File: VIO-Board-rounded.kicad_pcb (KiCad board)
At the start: 4 copper layers, 39.6 x 39.6 mm, 20 parts, among them J1 Conn_01x02_Female, J2 USB_B_Micro, J3 Conn_01x09_Male, J4 Conn_01x09_Male, J5 Conn_01x09_Male, J6 Conn_01x09_Female, J7 Conn_01x09_Female, J8 Conn_01x09_Female, U1 CP2102N-Axx-xQFN28

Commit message: ...
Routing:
- net /SYNC: track 52.6 -> 62.0 mm
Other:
- board text removed: "3v3"
- board text removed: "5v"
- board text removed: "GND"
- board text removed: "OPTO_GND"
- board text removed: "OPTO_IN"
- board text removed: "OPTO_OUT"
- board text removed: "RESTORE"
- board text removed: "RX1"
- board text removed: "RX2"
- board text removed: "SYNC"
- board text removed: "SYNC_IN"
- board text removed: "SYNC_OUT"
- board text removed: "TX"
- board text removed: "TX1"
- board text removed: "TX2"
- board text removed: "VS"

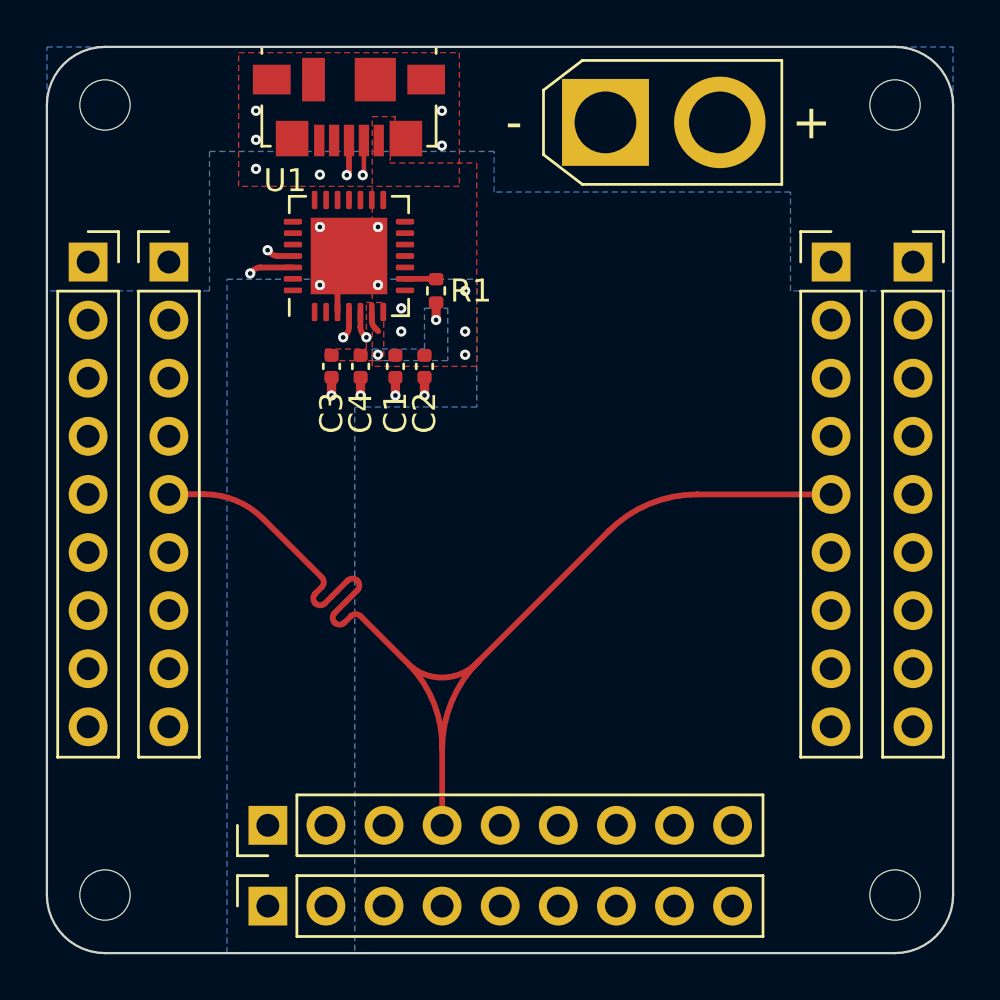
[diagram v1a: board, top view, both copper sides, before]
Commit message: new package, ESD protection, fixes
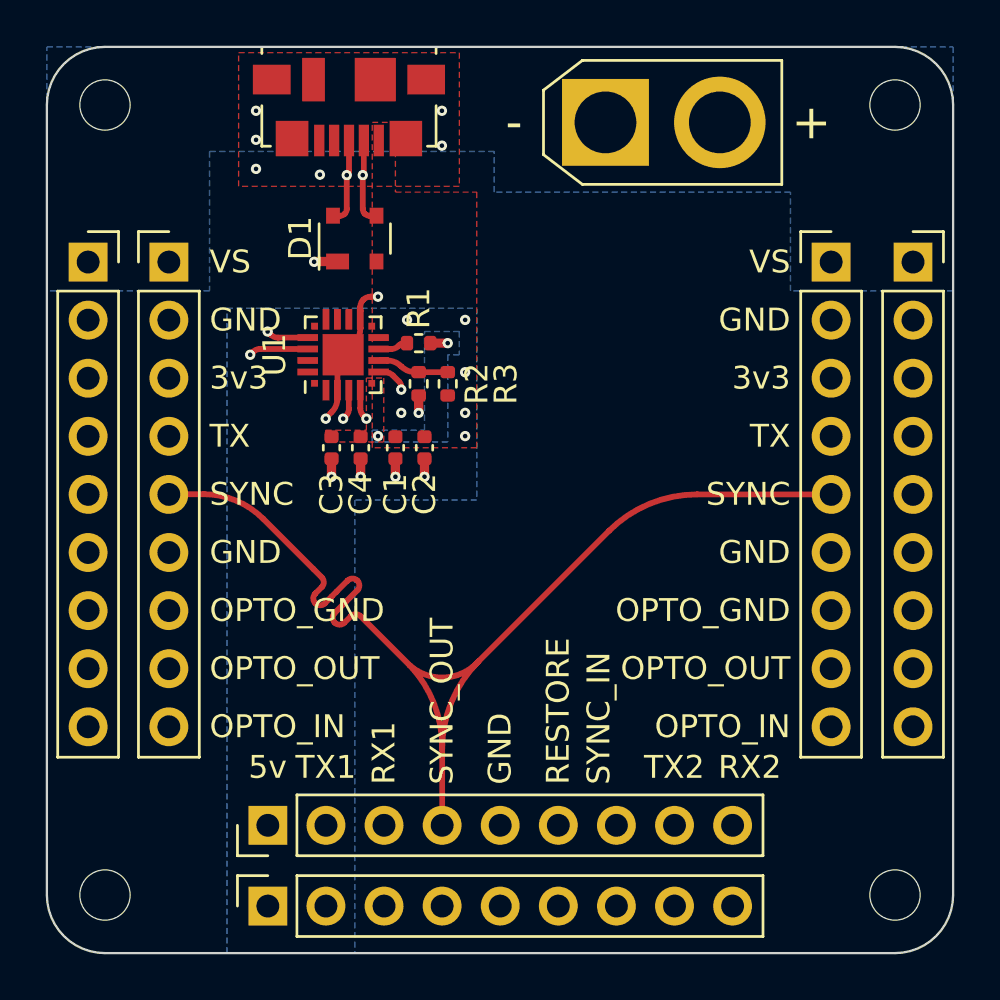
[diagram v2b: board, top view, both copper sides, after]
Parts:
- added D1: SP0503BAHT, Package_TO_SOT_SMD:SOT-143, F.Cu at (70.1, 59.2)
- added R2: 22k1, Resistor_SMD:R_0402_1005Metric, F.Cu at (74.2, 65.5)
- added R3: 47k5, Resistor_SMD:R_0402_1005Metric, F.Cu at (72.9, 65.5)
- U1: value CP2102N-Axx-xQFN28 -> CP2102N-Axx-xQFN20; footprint Package_DFN_QFN:QFN-28-1EP_5x5mm_P0.5mm_EP3.35x3.35mm -> Package_DFN_QFN:SiliconLabs_QFN-20-1EP_3x3mm_P0.5mm_EP1.8x1.8mm
- moved U1 4.33 mm to (69.6, 64.3)
- moved C1 3.56 mm to (71.9, 68.3)
- moved C2 3.56 mm to (73.2, 68.3)
- moved C3 3.56 mm to (69.1, 68.3)
- moved C4 3.56 mm to (70.4, 68.3)
- moved R1 2.41 mm to (72.9, 63.8), turned to 180 degrees
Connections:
- U1 pad 12: unconnected-(U1-Pad12) -> GNDREF
- U1 pad 17: unconnected-(U1-Pad17) -> /RX2
- U1 pad 18: unconnected-(U1-Pad18) -> /TX2
- U1 pad 21: unconnected-(U1-Pad21) -> GNDREF
- U1 pad 8: VBUS -> Net-(R2-Pad2)
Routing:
- net /D+: track 10.0 -> 16.0 mm
- net /D-: track 10.1 -> 15.9 mm
- net GNDREF: track 9.31 -> 14.9 mm
- net Net-(R2-Pad2): track 0.00 -> 3.15 mm
- net /TX2: track 36.8 -> 34.8 mm
- net VBUS: track 0.00 -> 1.42 mm, vias 5 -> 7
- net /RX2: track 37.8 -> 36.5 mm
- net +3V3: track 1.69 -> 0.76 mm
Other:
- board text added: "3v3"
- board text added: "5v"
- board text added: "GND"
- board text added: "OPTO_GND"
- board text added: "OPTO_IN"
- board text added: "OPTO_OUT"
- board text added: "RESTORE"
- board text added: "RX1"
- board text added: "RX2"
- board text added: "SYNC"
- board text added: "SYNC_IN"
- board text added: "SYNC_OUT"
- board text added: "TX"
- board text added: "TX1"
- board text added: "TX2"
- board text added: "VS"

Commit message: final touches
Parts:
- added G***: LOGO, Adin_Logo:Adin_Logo, B.Cu at (76.5, 72.9)
